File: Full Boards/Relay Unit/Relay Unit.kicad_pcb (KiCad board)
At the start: 4 copper layers, 320 x 80 mm, 158 parts, among them J3 Program Header, SW1 Status Switch, SW3 SW_MEC_5G, SW4 SW_MEC_5G, U1 ISO1044BD, U10 FM24CL64B-G, U15 LM1117MP-5.0, U2 MAX3232, U3 STM32C092KCT6, U4 ULN2003A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

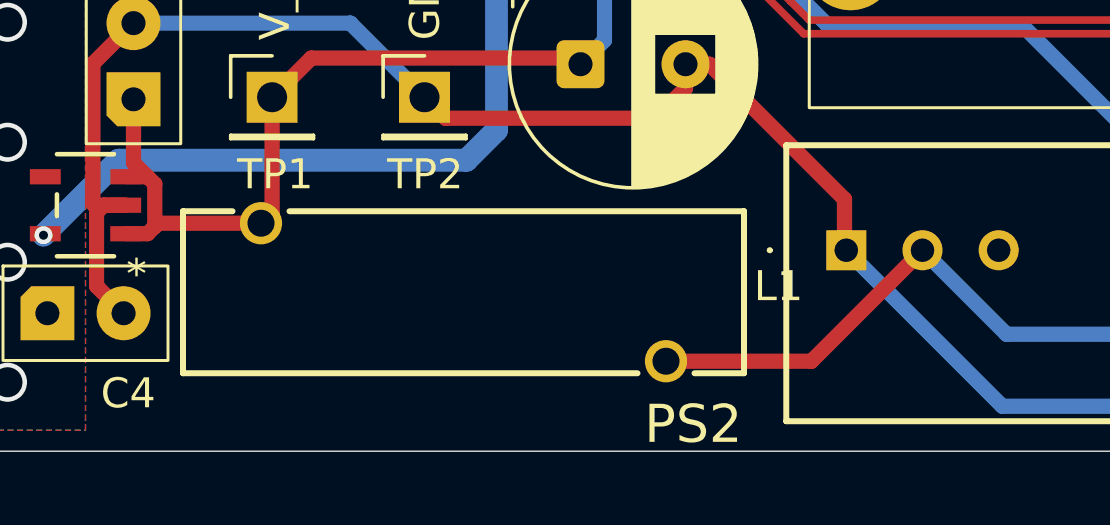
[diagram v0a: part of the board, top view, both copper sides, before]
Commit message: Updated PCBs to swap RVS diodes from SLD15-018 to SLD22-018. Also swapped out the inductor from 7847111100 to PA4340.103NLT.
Signed-off-by: Madison Kelly <digital.mermaid@gmail.com>
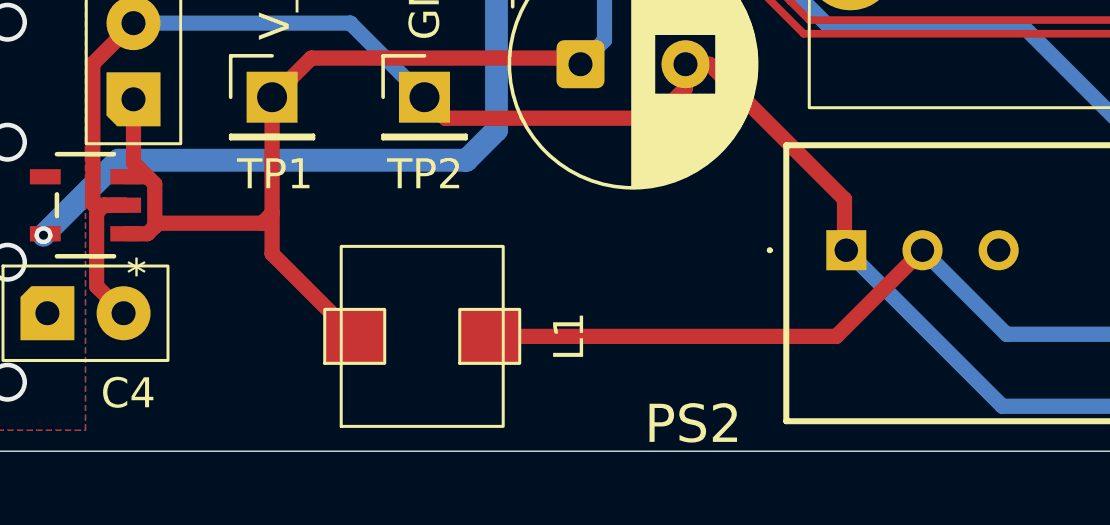
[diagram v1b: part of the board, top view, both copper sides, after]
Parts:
- D146: value SLD15-018 -> SLD22-018
- L1: value 7847111100 -> PA4340.103NLT; footprint mr-stuff:WE-RCIT_7847111100 -> mr-stuff:Pulse PA4340.103NLT
- moved L1 2.02 mm to (294.8, 129.5), turned to 90 degrees
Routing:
- net Net-(PS2-+VIN): track 31.0 -> 36.6 mm
- net V_RAW: track 92.1 -> 97.3 mm
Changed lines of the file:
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@@
 			(crossoutdnponfab yes)
 			(subtractmaskfromsilk no)
-			(outputformat 1)
+			(outputformat 4)
 			(mirror no)
 			(drillshape 0)
 			(scaleselection 1)
-			(outputdirectory "")
+			(outputdirectory "PDFs/")
 		)
 	)
@@
 			)
 		)
-		(property "Value" "SLD15-018"
+		(property "Value" "SLD22-018"
 			(at 0 0 0)
 			(layer "F.SilkS")
@@
 		)
 	)
+	(footprint "mr-stuff:Pulse PA4340.103NLT"
+		(layer "F.Cu")
+		(at 294.8 129.5 90)
+		(property "Reference" "L1"
+			(at 0 4.9 90)
+			(unlocked yes)
+			(layer "F.SilkS")
+			(effects
+				(font
+					(size 1 1)
+					(thickness 0.1)
+				)
+			)
+		)
+		(property "Value" "PA4340.103NLT"
+			(at 0 6.4 90)
+			(unlocked yes)
+			(layer "F.Fab")
+			(effects
+				(font
+					(size 1 1)
+					(thickness 0.15)
+				)
+			)
+		)
+		(property "Datasheet" "~"
+			(at 0 0 90)
+			(unlocked yes)
+			(layer "F.Fab")
+			(hide yes)
+			(effects
+				(font
+					(size 1 1)
+					(thickness 0.15)
+				)
+			)
+		)
+		(property "Description" "Inductor"
+			(at 0 0 90)
+			(unlocked yes)
+			(layer "F.Fab")
+			(hide yes)
+			(effects
+				(font
+					(size 1 1)
+					(thickness 0.15)
+				)
+			)
+		)
+		(property ki_fp_filters "Choke_* *Coil* Inductor_* L_*")
+		(sheetname "/")
+		(sheetfile "Relay Unit.kicad_sch")
+		(attr board_only exclude_from_pos_files)
+		(fp_rect
+			(start -0.9 -3.25)
+			(end 0.9 -1.25)
+			(stroke
+				(width 0.1)
+				(type solid)
+			)
+			(fill no)
+			(layer "F.SilkS")
+		)
+		(fp_rect
+			(start -3 -2.7)
+			(end 3 2.7)
+			(stroke
+				(width 0.1)
+				(type solid)
+			)
+			(fill no)
+			(layer "F.SilkS")
+		)
+		(fp_rect
+			(start -0.9 1.25)
+			(end 0.9 3.25)
+			(stroke
+				(width 0.1)
+				(type solid)
+			)
+			(fill no)
+			(layer "F.SilkS")
+		)
+		(fp_text user "${REFERENCE}"
+			(at 0 7.9 90)
+			(unlocked yes)
+			(layer "F.Fab")
+			(effects
+				(font
+					(size 1 1)
+					(thickness 0.15)
+				)
+			)
+		)
+		(pad "1" smd roundrect
+			(at 0 -2.25 90)
+			(size 1.8 2)
+			(layers "F.Cu" "F.Mask" "F.Paste")
+			(roundrect_rratio 0.05)
+			(net 5 "V_RAW")
+			(pinfunction "1")
+			(pintype "passive")
+		)
+		(pad "2" smd roundrect
+			(at 0 2.25 90)
+			(size 1.8 2)
+			(layers "F.Cu" "F.Mask" "F.Paste")
+			(roundrect_rratio 0.05)
+			(net 7 "Net-(PS2-+VIN)")
+			(pinfunction "2")
+			(pintype "passive")
+		)
+		(embedded_fonts no)
+		(model "${MY_3DMODELS}/Pulse PA4340.103NLT/PA4340.103NLT.STEP"
+			(offset
+				(xyz 0 0 0)
+			)
+			(scale
+				(xyz 1 1 1)
+			)
+			(rotate
+				(xyz -90 -0 -0)
+			)
+		)
+	)
 	(footprint "Resistor_THT:R_Axial_DIN0207_L6.3mm_D2.5mm_P7.62mm_Horizontal"
 		(layer "F.Cu")
@@
 		)
 	)
-	(footprint "mr-stuff:WE-RCIT_7847111100"
-		(layer "F.Cu")
-		(at 296.176342 128.028)
-		(property "Reference" "L1"
-			(at 10.5 -0.2 0)
-			(layer "F.SilkS")
-			(effects
-				(font
-					(size 1 1)
-					(thickness 0.15)
-				)
-			)
-		)
-		(property "Value" "7847111100"
-			(at -0.576342 4.172 0)
-			(layer "Dwgs.User")
-			(effects
-				(font
-					(size 1 1)
-					(thickness 0.15)
-				)
-			)
-		)
-		(property "Datasheet" "https://www.we-online.com/components/products/datasheet/7847111100.pdf"
-			(at 0 0 0)
-			(layer "F.Fab")
-			(hide yes)
-			(effects
-				(font
-					(size 1.27 1.27)
-					(thickness 0.15)
-				)
-			)
-		)
-		(property "Description" "10uH, 3A, rod-core inductor"
-			(at 0 0 0)
-			(layer "F.Fab")
-			(hide yes)
-			(effects
-				(font
-					(size 1.27 1.27)
-					(thickness 0.15)
-				)
-			)
-		)
-		(sheetname "/")
-		(sheetfile "Relay Unit.kicad_sch")
-		(attr through_hole)
-		(fp_line
-			(start -9.35 -2.7)
-			(end -9.35 2.7)
-			(stroke
-				(width 0.2)
-				(type solid)
-			)
-			(layer "F.SilkS")
-		)
-		(fp_line
-			(start -9.35 2.7)
-			(end 5.8 2.7)
-			(stroke
-				(width 0.2)
-				(type solid)
-			)
-			(layer "F.SilkS")
-		)
-		(fp_line
-			(start -7.7 -2.7)
-			(end -9.35 -2.7)
-			(stroke
-				(width 0.2)
-				(type solid)
-			)
-			(layer "F.SilkS")
-		)
-		(fp_line
-			(start -5.8 -2.7)
-			(end 9.35 -2.7)
-			(stroke
-				(width 0.2)
-				(type solid)
-			)
-			(layer "F.SilkS")
-		)
-		(fp_line
-			(start 9.35 -2.7)
-			(end 9.35 2.7)
-			(stroke
-				(width 0.2)
-				(type solid)
-			)
-			(layer "F.SilkS")
-		)
-		(fp_line
-			(start 9.35 2.7)
-			(end 7.7 2.7)
-			(stroke
-				(width 0.2)
-				(type solid)
-			)
-			(layer "F.SilkS")
-		)
-		(fp_poly
-			(pts
-				(xy -9.55 -3.2) (xy 9.55 -3.2) (xy 9.55 3.2) (xy -9.55 3.2)
-			)
-			(stroke
-				(width 0.1)
-				(type solid)
-			)
-			(fill yes)
-			(layer "F.CrtYd")
-		)
-		(fp_line
-			(start -9.25 -2.6)
-			(end 9.25 -2.6)
-			(stroke
-				(width 0.1)
-				(type solid)
-			)
-			(layer "F.Fab")
-		)
-		(fp_line
-			(start -9.25 2.6)
-			(end -9.25 -2.6)
-			(stroke
-				(width 0.1)
-				(type solid)
-			)
-			(layer "F.Fab")
-		)
-		(fp_line
-			(start 9.25 -2.6)
-			(end 9.25 2.6)
-			(stroke
-				(width 0.1)
-				(type solid)
-			)
-			(layer "F.Fab")
-		)
-		(fp_line
-			(start 9.25 2.6)
-			(end -9.25 2.6)
-			(stroke
-				(width 0.1)
-				(type solid)
-			)
-			(layer "F.Fab")
-		)
-		(pad "1" thru_hole circle
-			(at -6.75 -2.3)
-			(size 1.408 1.408)
-			(drill 0.9)
-			(layers "*.Cu" "*.Mask")
-			(remove_unused_layers no)
-			(net 5 "V_RAW")
-			(pintype "passive")
-			(solder_mask_margin 0.102)
-		)
-		(pad "2" thru_hole circle
-			(at 6.75 2.3)
-			(size 1.408 1.408)
-			(drill 0.9)
-			(layers "*.Cu" "*.Mask")
-			(remove_unused_layers no)
-			(net 7 "Net-(PS2-+VIN)")
-			(pintype "passive")
-			(solder_mask_margin 0.102)
-		)
-		(embedded_fonts no)
-		(model "${MY_3DMODELS}/Würth 7847111100/Download_STP_WE-RCIT-7847111100+%28rev1%29.stp"
-			(offset
-				(xyz 0 0 3)
-			)
-			(scale
-				(xyz 1 1 1)
-			)
-			(rotate
-				(xyz -0 -0 -90)
-			)
-		)
-	)
 	(footprint "mr-stuff:Keystone 7799"
 		(layer "F.Cu")
@@
 	)
 	(segment
+		(start 289.796342 125.398)
+		(end 289.796342 126.746342)
+		(width 0.508)
+		(layer "F.Cu")
+		(net 5)
+	)
+	(segment
 		(start 284.916192 124.177999)
 		(end 285.644541 124.177999)
@@
 	)
 	(segment
+		(start 289.796342 125.398)
+		(end 289.466342 125.728)
+		(width 0.508)
+		(layer "F.Cu")
+		(net 5)
+	)
+	(segment
 		(start 285.246342 121.528)
 		(end 285.176342 121.598)
@@
 	)
 	(segment
-		(start 285.644541 124.177999)
-		(end 285.885542 124.419)
+		(start 289.796342 126.746342)
+		(end 292.55 129.5)
 		(width 0.508)
 		(layer "F.Cu")
@@
 	)
 	(segment
-		(start 289.796342 125.398)
-		(end 289.466342 125.728)
+		(start 285.644541 124.177999)
+		(end 285.885542 124.419)
 		(width 0.508)
 		(layer "F.Cu")
@@
 	)
 	(segment
-		(start 302.926342 130.328)
-		(end 307.776342 130.328)
+		(start 297.05 129.5)
+		(end 308.604342 129.5)
 		(width 0.508)
 		(layer "F.Cu")
@@
 	)
 	(segment
-		(start 307.776342 130.328)
+		(start 308.604342 129.5)
 		(end 311.476342 126.628)
 		(width 0.508)

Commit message: Updated boards and schematics.
These are the version that have been ordered. Any further changes will be a new version.

Signed-off-by: Madison Kelly <digital.mermaid@gmail.com>
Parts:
- removed D147, D148, D30, D31, D32, D33, D34, D35, D36, D37, D38, D39, D40, D41, D42, D43, D44, D45, D46, D47: 1N5822, Diode_THT:D_DO-41_SOD81_P10.16mm_Horizontal
- added C25: 0.1uF, mr-stuff:RCE5C1H104J2A2H03B, F.Cu at (91.3, 115.6)
- added J1: Future Bond, Connector_PinHeader_2.54mm:PinHeader_1x03_P2.54mm_Vertical, F.Cu at (308.7, 110.4)
- added R10: 3.3K, Resistor_THT:R_Axial_DIN0207_L6.3mm_D2.5mm_P7.62mm_Horizontal, F.Cu at (54.7, 72.5)
- added R11: 3.3K, Resistor_THT:R_Axial_DIN0207_L6.3mm_D2.5mm_P7.62mm_Horizontal, F.Cu at (54.7, 69.5)
- C7: value TDK FA28NP01H152JNU06 -> 0.1uF; footprint mr-stuff:TDK CAPRB500W50L400T250H550 -> mr-stuff:RCE5C1H104J2A2H03B
- R68: value 10 -> 475
- moved C7 31.4 mm to (303.0, 126.5), turned to 180 degrees
- moved TVS1 5.73 mm to (96.7, 115.0), turned to 180 degrees
- moved C10 3.60 mm to (204.2, 117.9)
- moved C11 2.12 mm to (211.1, 118.9)
- moved C19 1.38 mm to (75.0, 126.2)
- moved C21 1.33 mm to (83.0, 125.1)
- moved R5 1.03 mm to (86.4, 123.4)
- moved R4 0.95 mm to (89.5, 123.4)
- moved R1 0.85 mm to (92.6, 131.0)
- moved R6 0.75 mm to (95.7, 123.4)
- moved C15 0.68 mm to (101.9, 125.5)
- moved R3 0.64 mm to (98.8, 131.0)
- moved C14 0.58 mm to (105.2, 125.5)
- moved DE1 0.11 mm to (200.4, 123.7)
- moved C12 0.05 mm to (205.4, 113.2)
- renumbered N2K2 to N2K1
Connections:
- C7 pad 1: GND -> GND_SHIP
- C7 pad 2: GND_SHIP -> GND
- N2K1 pad 1: unconnected-(N2K2-Shield-Pad1) -> Net-(J1-Pin_1)
- U2 pad 10: unconnected-(U2-T2IN-Pad10) -> +3.3V
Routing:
- net /CA5: track 295.1 -> 224.3 mm
- net /CA6: track 292.9 -> 228.1 mm
- net Net-(J1-Pin_1): track 0.00 -> 51.1 mm, vias 0 -> 1
- net /CA7: track 291.4 -> 246.5 mm
- net /CA8: track 287.1 -> 248.3 mm
- net /CA9: track 287.7 -> 253.3 mm
- net +3.3V: track 520.9 -> 545.1 mm
- net GND_SHIP: track 654.3 -> 676.8 mm
- net Net-(U6-O3): track 201.2 -> 185.3 mm
- net /BOARD_I2C_SDA: track 123.9 -> 139.0 mm
- net Net-(U5-O3): track 127.3 -> 112.8 mm
- net Net-(U4-O5): track 80.8 -> 66.5 mm
- net Net-(U6-O5): track 225.0 -> 211.7 mm
- net Net-(U5-O5): track 153.5 -> 140.3 mm
- net Net-(U5-O1): track 99.6 -> 86.8 mm
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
